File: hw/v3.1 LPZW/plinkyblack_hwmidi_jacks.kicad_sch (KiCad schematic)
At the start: 300 parts, among them J1 AudioJack2_SwitchT, J10 AudioJack2_SwitchT, J11 AudioJack2_SwitchT, J12 Conn_02x08_Odd_Even, J13 Conn_02x08_Odd_Even, J14 AudioJack2_SwitchT, J15 AudioJack2_SwitchT, J16 AudioJack2_SwitchT, J17 AudioJack2_SwitchT, J2 AudioJack2_SwitchT, J20 oled0.91, J22 AudioJack2_SwitchT, J23 AudioJack2_SwitchT, J25 Conn_01x16_Female, J28 PJ313, J29 PJ313, J3 AudioJack2_SwitchT, J30 PJ313, J31 PJ313, J32 PJ313, J33 PJ313, J4 AudioJack2_SwitchT, J5 SWD header, J6 AudioJack2_SwitchT, J7 AudioJack2_SwitchT, J8 AudioJack2_SwitchT, J9 AudioJack2_SwitchT, Q1 MMBT3904, U1 HCPL-0631-500E, U1 MCP6002-xSN, U10 TL072, U11 TL072, U12 W25Q32JVSS, U13 TPS61040DBV, U14 W25Q32JVSS, U15 WE-TVS-824001, U16 TL072, U17 LIS2DH12, U18 TL072, U19 TYPE-C-31-M-14, U2 LM1117-3.3, U20 TYPE-C-31-M-14, U22 PI3USB102EZLE, U23 WE-TVS-824001, U3 LM1117-3.3, U4 STM32L476VGT6, U5 TL072, U6 WM8758B, U7 TL072, U8 MCP6002-xSN, U9 MCP6002-xSN, Y1 Crystal_GND24

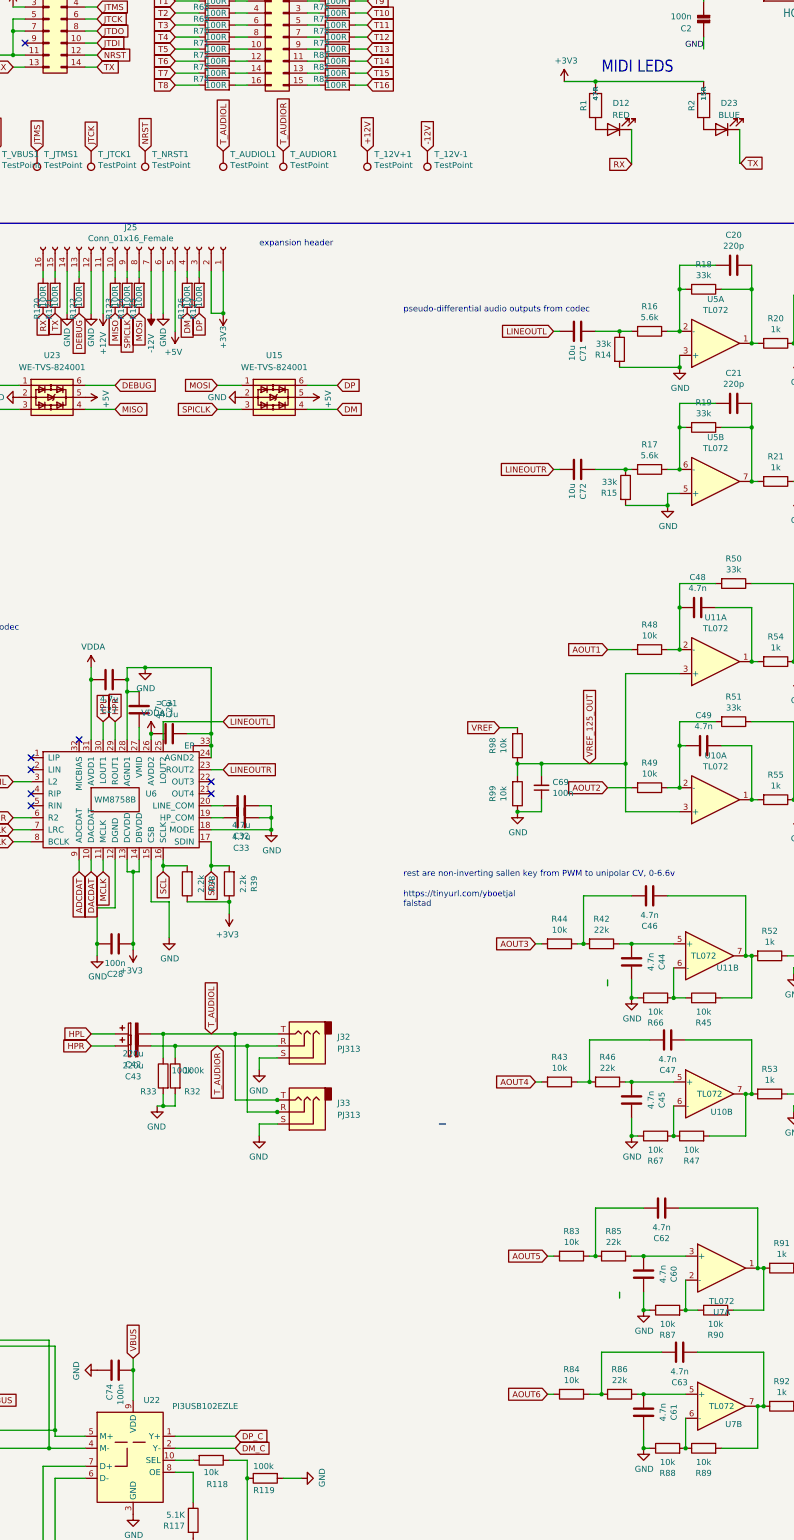
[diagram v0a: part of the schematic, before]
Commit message: no DRC errors, but not confirmed working
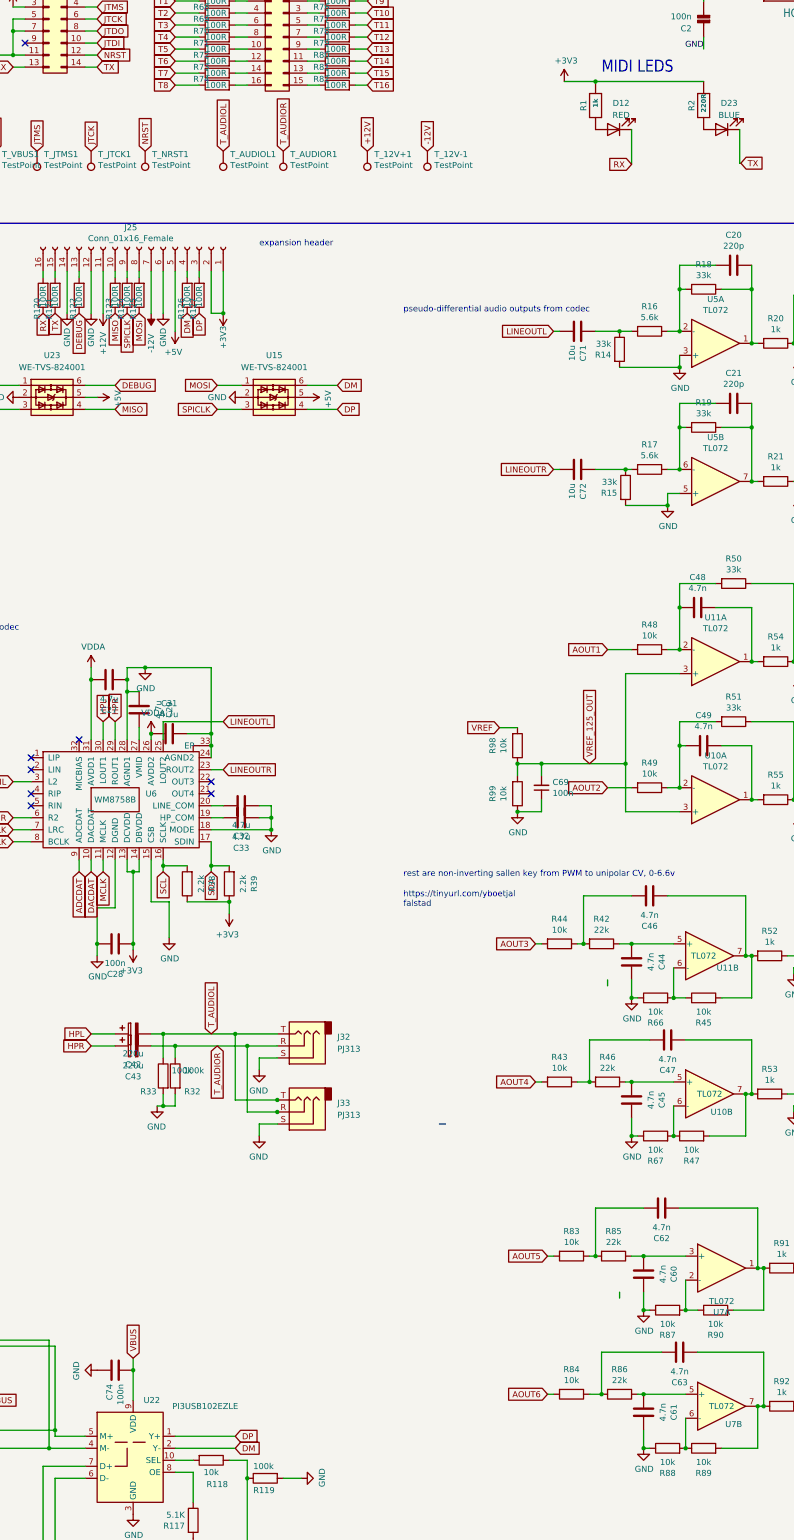
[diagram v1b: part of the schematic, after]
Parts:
- R1: value 47R -> 1k; LCSC C23182 -> C21190
- R2: value 15R -> 220R; LCSC C22810 -> C22962
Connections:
- net DM_C is gone; now on net DM: U22.2 (Y-)
- net DP_C is gone; now on net DP: U22.1 (Y+)
- net DM: now also U15.6; no longer U15.4
- net DP: now also U15.4; no longer U15.6
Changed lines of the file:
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@@
     (stroke (width 0) (type default))
   )
-  (wire (pts (xy 382.27 124.46) (xy 388.62 124.46))
+  (wire (pts (xy 382.27 129.54) (xy 388.62 129.54))
     (stroke (width 0) (type default))
   )
@@
     (stroke (width 0) (type default))
   )
-  (wire (pts (xy 382.27 129.54) (xy 388.62 129.54))
+  (wire (pts (xy 382.27 124.46) (xy 388.62 124.46))
     (stroke (width 0) (type default))
   )
@@
     (stroke (width 0) (type default))
   )
+  (wire (pts (xy 337.82 127) (xy 335.28 127))
+    (stroke (width 0) (type default))
+  )
   (wire (pts (xy 210.82 237.49) (xy 215.9 237.49))
     (stroke (width 0) (type default))
@@
     )
   )
-  (global_label "DM" (shape input) (at 388.62 129.54 0)
+  (global_label "DM" (shape input) (at 388.62 124.46 0)
     (effects (font (size 1.27 1.27)) (justify left))
-    (property "Intersheetrefs" "${INTERSHEET_REFS}" (at 388.62 129.54 0)
+    (property "Intersheetrefs" "${INTERSHEET_REFS}" (at 388.62 124.46 0)
       (effects (font (size 1.27 1.27)) hide)
     )
@@
     )
   )
-  (global_label "DP" (shape input) (at 388.62 124.46 0)
+  (global_label "DP" (shape input) (at 388.62 129.54 0)
     (effects (font (size 1.27 1.27)) (justify left))
-    (property "Intersheetrefs" "${INTERSHEET_REFS}" (at 388.62 124.46 0)
+    (property "Intersheetrefs" "${INTERSHEET_REFS}" (at 388.62 129.54 0)
       (effects (font (size 1.27 1.27)) hide)
     )
@@
     )
   )
-  (global_label "DM_C" (shape input) (at 367.03 349.25 0)
+  (global_label "DM" (shape input) (at 367.03 349.25 0)
     (effects (font (size 1.27 1.27)) (justify left))
     (property "Intersheetrefs" "${INTERSHEET_REFS}" (at 367.03 349.25 0)
@@
     )
   )
-  (global_label "DP_C" (shape input) (at 367.03 346.71 0)
+  (global_label "DP" (shape input) (at 367.03 346.71 0)
     (effects (font (size 1.27 1.27)) (justify left))
     (property "Intersheetrefs" "${INTERSHEET_REFS}" (at 367.03 346.71 0)
@@
       (effects (font (size 1.27 1.27)))
     )
-    (property "Value" "15R" (at 466.09 62.738 0)
+    (property "Value" "220R" (at 466.09 64.77 0)
       (effects (font (size 1.016 1.016) bold))
     )
@@
       (effects (font (size 1.27 1.27)) hide)
     )
-    (property "LCSC" "C22810" (at 466.09 65.278 0)
+    (property "LCSC" "C22962" (at 466.09 65.278 0)
       (effects (font (size 1.27 1.27)) hide)
     )
@@
       (effects (font (size 1.27 1.27)))
     )
-    (property "Value" "47R" (at 443.23 62.738 0)
+    (property "Value" "1k" (at 443.23 64.77 0)
       (effects (font (size 1.016 1.016) bold))
     )
@@
       (effects (font (size 1.27 1.27)) hide)
     )
-    (property "LCSC" "C23182" (at 443.23 65.278 0)
+    (property "LCSC" "C21190" (at 443.23 65.278 0)
       (effects (font (size 1.27 1.27)) hide)
     )
@@
     )
   )
-  (symbol (lib_id "power:+5V") (at 335.28 127 270) (unit 1)
+  (symbol (lib_id "power:+5V") (at 337.82 127 270) (unit 1)
     (in_bom yes) (on_board yes) (dnp no)
-    (property "Reference" "#PWR080" (at 331.47 127 0)
+    (property "Reference" "#PWR080" (at 334.01 127 0)
       (effects (font (size 1.27 1.27)) hide)
     )
-    (property "Value" "+5V" (at 339.6742 127.381 0)
+    (property "Value" "+5V" (at 342.2142 127.381 0)
       (effects (font (size 1.27 1.27)))
     )
-    (property "Footprint" "" (at 335.28 127 0)
+    (property "Footprint" "" (at 337.82 127 0)
       (effects (font (size 1.27 1.27)) hide)
     )
-    (property "Datasheet" "" (at 335.28 127 0)
+    (property "Datasheet" "" (at 337.82 127 0)
       (effects (font (size 1.27 1.27)) hide)
     )

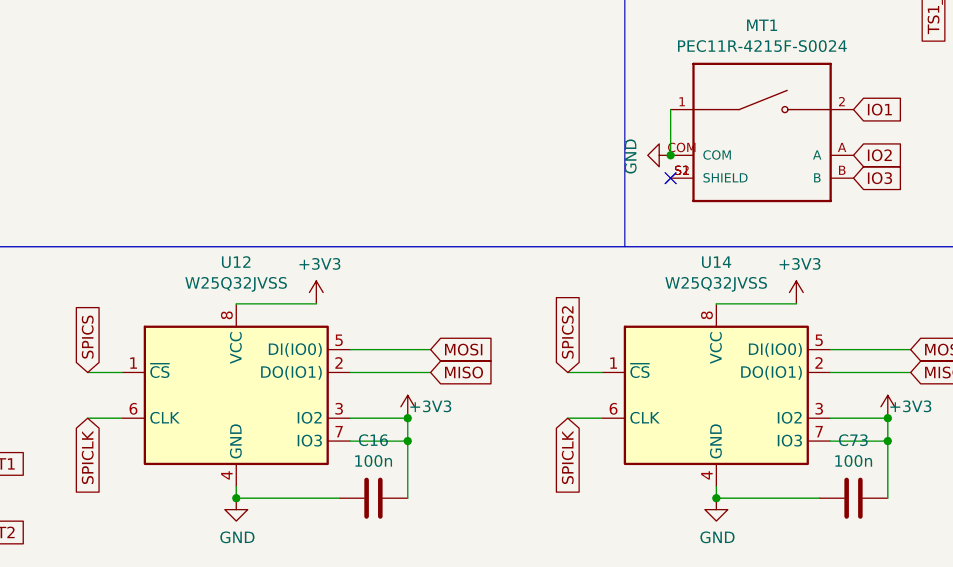
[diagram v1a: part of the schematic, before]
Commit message: Updated flash chip value from W25Q32JVSS to W25Q128JVSIQ
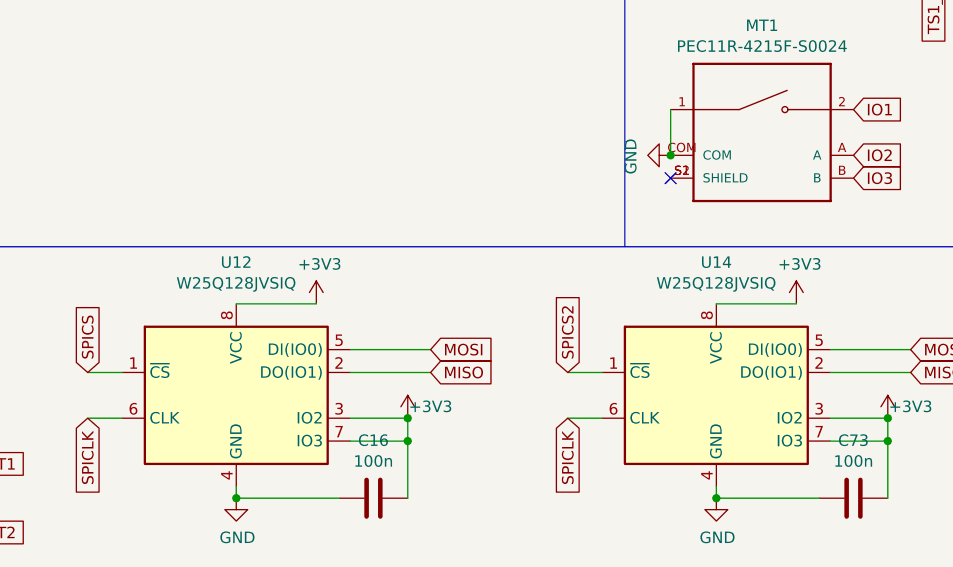
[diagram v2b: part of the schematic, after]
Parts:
- U12, U14: value W25Q32JVSS -> W25Q128JVSIQ
